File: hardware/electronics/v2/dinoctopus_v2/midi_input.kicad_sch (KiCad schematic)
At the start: 7 parts, among them J1-I1 SJ-3524-SMT, U3 H11L1

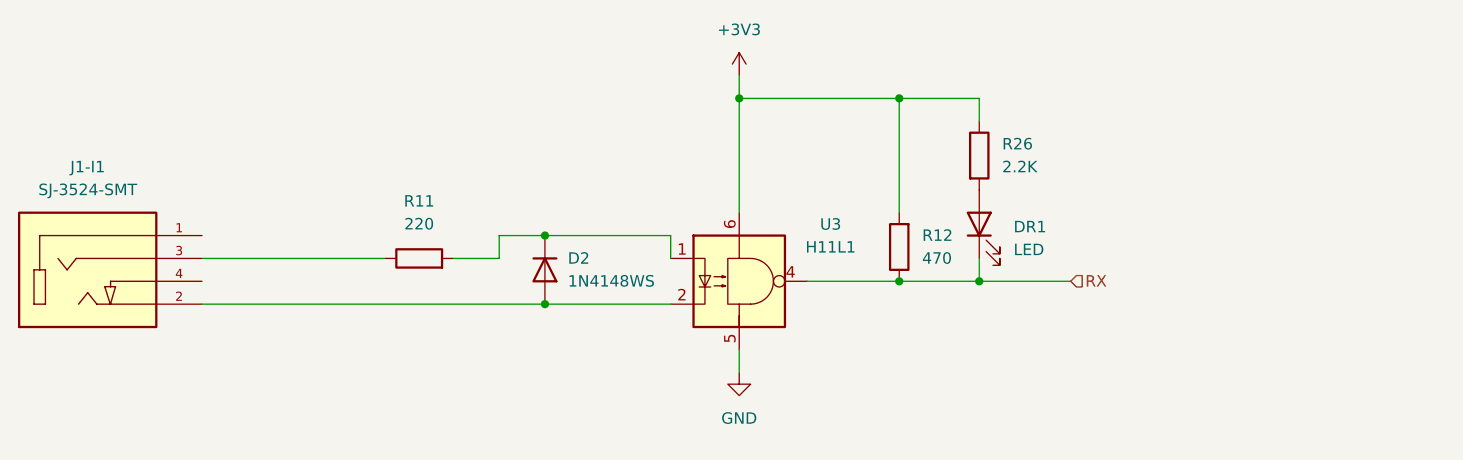
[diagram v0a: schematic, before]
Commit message: Rework schemas with JLCPCB references
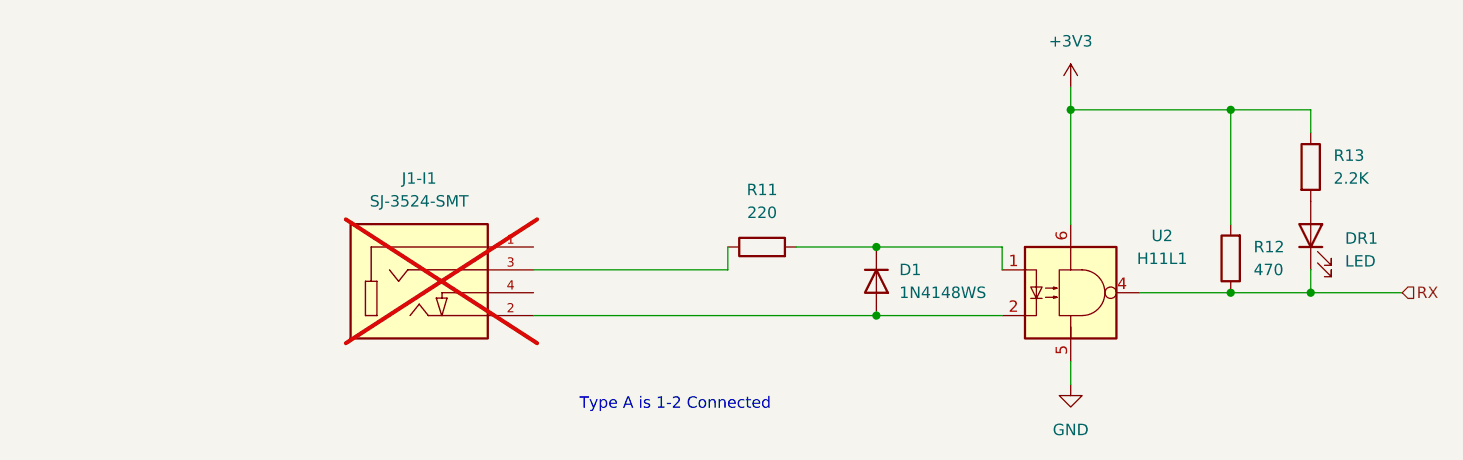
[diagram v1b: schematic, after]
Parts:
- removed D2: 1N4148WS, Diode_SMD:D_SOD-323, symbol Diode:1N4148WS
- removed R26: 2.2K, Resistor_SMD:R_1206_3216Metric_Pad1.30x1.75mm_HandSolder, symbol Device:R
- removed U3: H11L1, Package_DIP:SMDIP-6_W9.53mm, symbol Isolator:H11L1
- added D1: 1N4148WS, Diode_SMD:D_SOD-323, symbol Diode:1N4148WS
- added R13: 2.2K, Resistor_SMD:R_0805_2012Metric, symbol Device:R
- added U2: H11L1, Package_DIP:SMDIP-6_W9.53mm, symbol Isolator:H11L1
- DR1: footprint LED_SMD:LED_0805_2012Metric -> LED_SMD:LED_0603_1608Metric; LCSC (none) -> C2286
- J1-I1: footprint MIDI_projects:CUI_SJ-3524-SMT -> Library:CUI_SJ-3524-SMT; now not fitted; now left out of the parts list
- R11: footprint Resistor_SMD:R_1206_3216Metric_Pad1.30x1.75mm_HandSolder -> Resistor_SMD:R_0805_2012Metric; LCSC (none) -> C17557
- R12: footprint Resistor_SMD:R_1206_3216Metric_Pad1.30x1.75mm_HandSolder -> Resistor_SMD:R_0805_2012Metric; LCSC (none) -> C17710
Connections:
- net +3V3: now also R13.1, U2.6
- net GND: now also U2.5
- net RX: now also U2.4
- net at DR1.2 (A): now also R13.2
- net at R11.2: now also D1.1 (K), U2.1
- net at J1-I1.2: now also D1.2 (A), U2.2
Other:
- note added: "Type A is 1-2 Connected"
